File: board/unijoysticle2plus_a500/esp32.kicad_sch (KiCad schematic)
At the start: 17 parts, among them Q1 S8050, Q2 S8050, SW1 RESET, SW2 BOOT, U1 ESP32-WROOM-32E

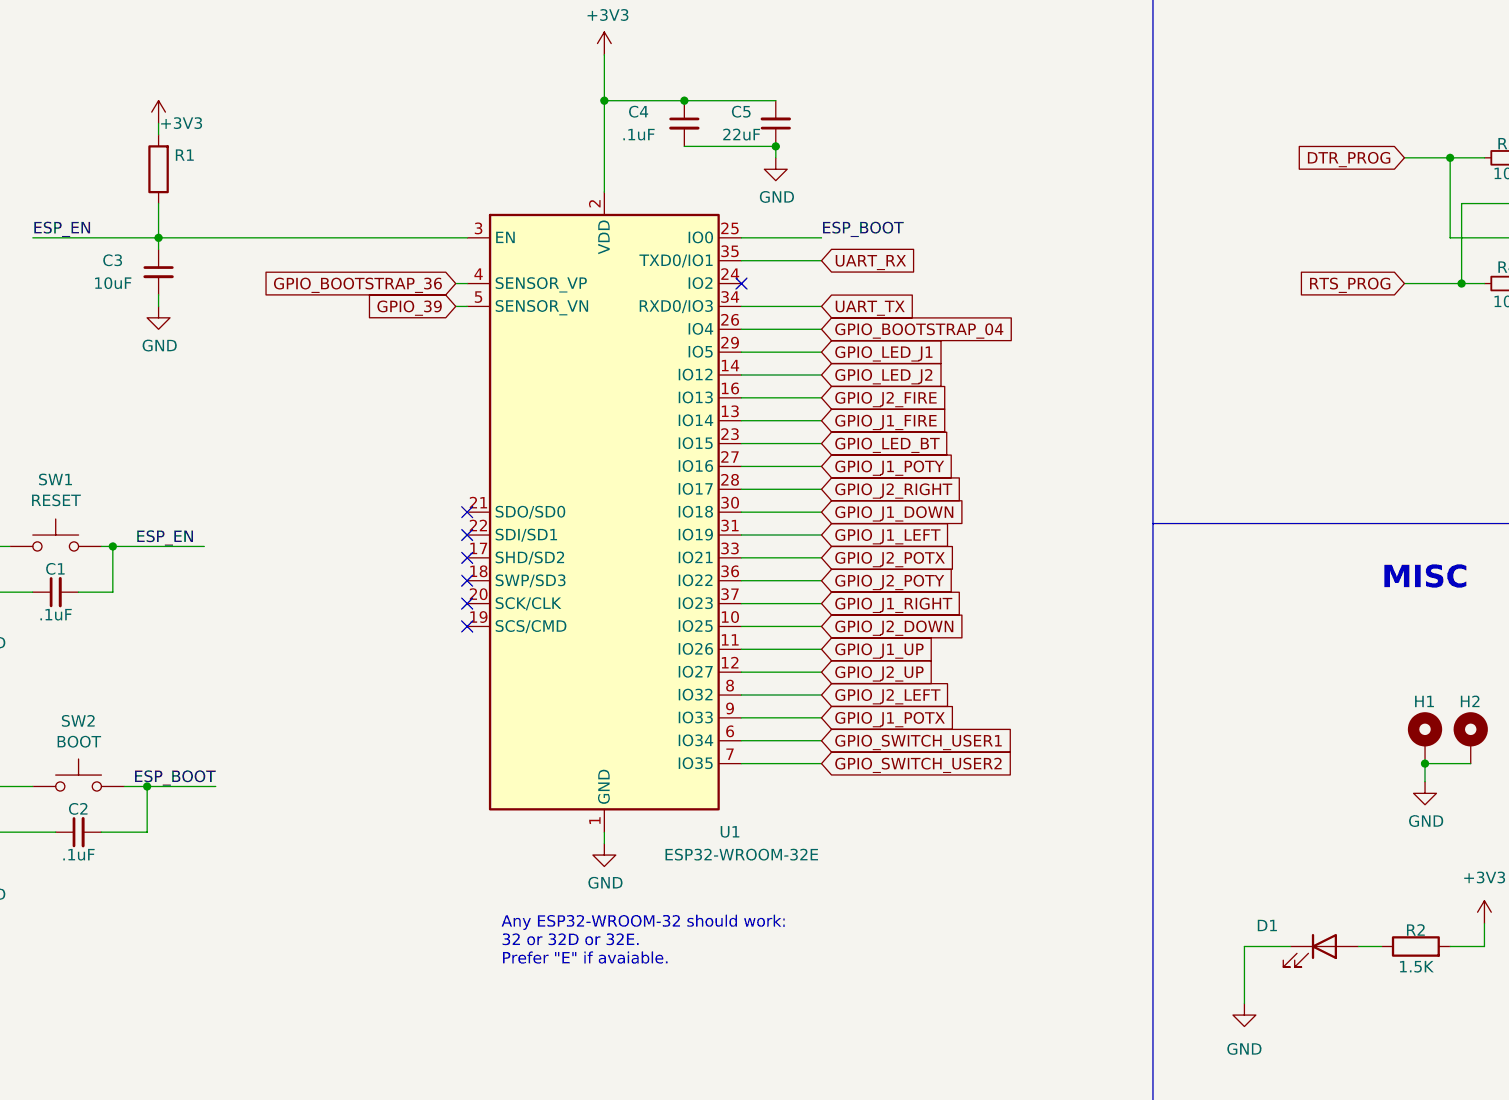
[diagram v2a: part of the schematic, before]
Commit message: uni a500: manual routing
WIP... all wires connected. requires to double check everything
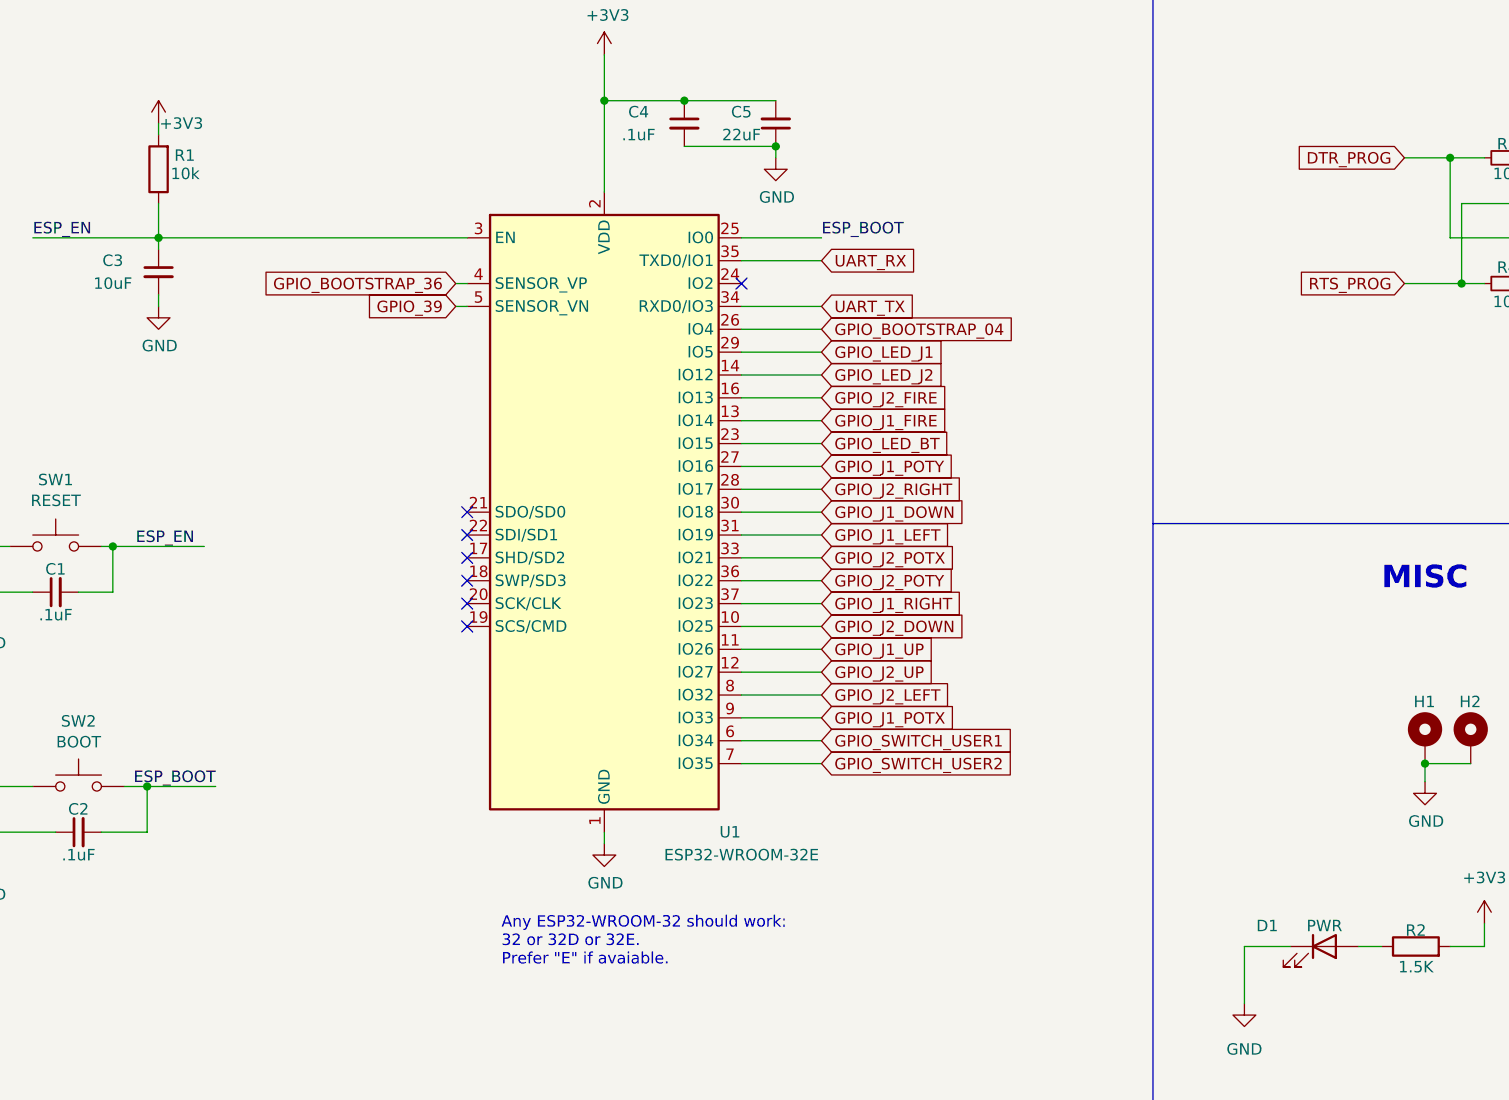
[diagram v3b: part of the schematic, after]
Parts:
- D1: value (none) -> PWR; footprint (none) -> LED_SMD:LED_0805_2012Metric_Pad1.15x1.40mm_HandSolder
- R1: value (none) -> 10k; footprint (none) -> Resistor_SMD:R_0805_2012Metric_Pad1.20x1.40mm_HandSolder
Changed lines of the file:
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@@
       (effects (font (size 1.27 1.27)) (justify left))
     )
-    (property "Value" "" (id 1) (at 42.672 44.958 0)
+    (property "Value" "10k" (id 1) (at 42.672 44.958 0)
       (effects (font (size 1.27 1.27)) (justify left))
     )
-    (property "Footprint" "" (id 2) (at 39.878 44.45 90)
+    (property "Footprint" "Resistor_SMD:R_0805_2012Metric_Pad1.20x1.40mm_HandSolder" (id 2) (at 39.878 44.45 90)
       (effects (font (size 1.27 1.27)) hide)
     )
@@
     (in_bom yes) (on_board yes)
     (property "Reference" "D1" (id 0) (at 161.29 128.524 0))
-    (property "Value" "" (id 1) (at 167.64 128.524 0))
-    (property "Footprint" "" (id 2) (at 167.64 130.81 0)
-      (effects (font (size 1.27 1.27)) hide)
-    )
+    (property "Value" "PWR" (id 1) (at 167.64 128.524 0))
+    (property "Footprint" "LED_SMD:LED_0805_2012Metric_Pad1.15x1.40mm_HandSolder" (id 2) (at 167.64 130.81 0)
+      (effects (font (size 1.27 1.27)) hide)
+    )

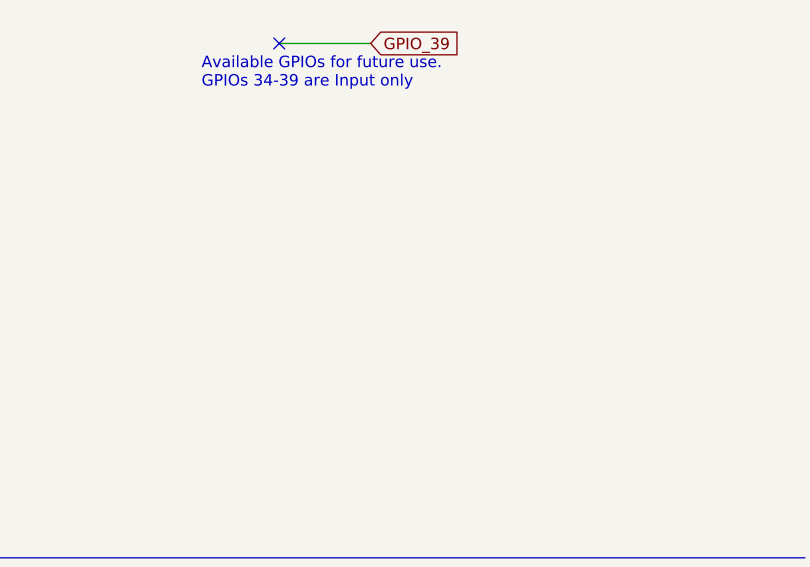
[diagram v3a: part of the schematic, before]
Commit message: Uni 2+ A500: many little changes
- replace resistor 0 with solder jumper for strapping pins
- move big cap a big down
- improved routing
- move vias outside pads
... and more
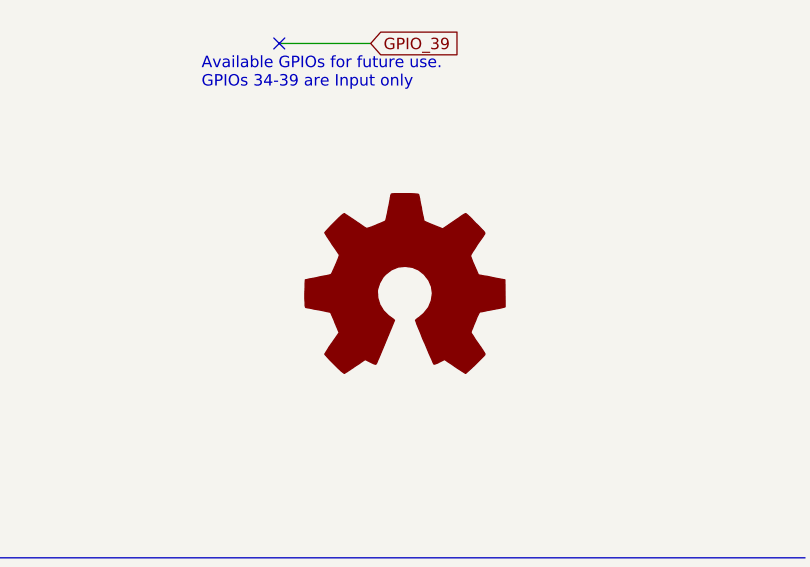
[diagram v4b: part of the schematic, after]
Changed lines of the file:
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@@
     (pin "1")
+  )
+  (symbol (lib_id "Graphic:Logo_Open_Hardware_Large") (at 240.03 124.46 0) (unit 1)
+    (in_bom yes) (on_board yes) (fields_autoplaced)
+    (property "Reference" "#LOGO1" (id 0) (at 240.03 111.76 0)
+      (effects (font (size 1.27 1.27)) hide)
+    )
+    (property "Value" "" (id 1) (at 240.03 134.62 0)
+      (effects (font (size 1.27 1.27)) hide)
+    )
+    (property "Footprint" "" (id 2) (at 240.03 124.46 0)
+      (effects (font (size 1.27 1.27)) hide)
+    )
+    (property "Datasheet" "~" (id 3) (at 240.03 124.46 0)
+      (effects (font (size 1.27 1.27)) hide)
+    )
   )
   (symbol (lib_id "power:GND") (at 158.75 137.16 0) (unit 1)

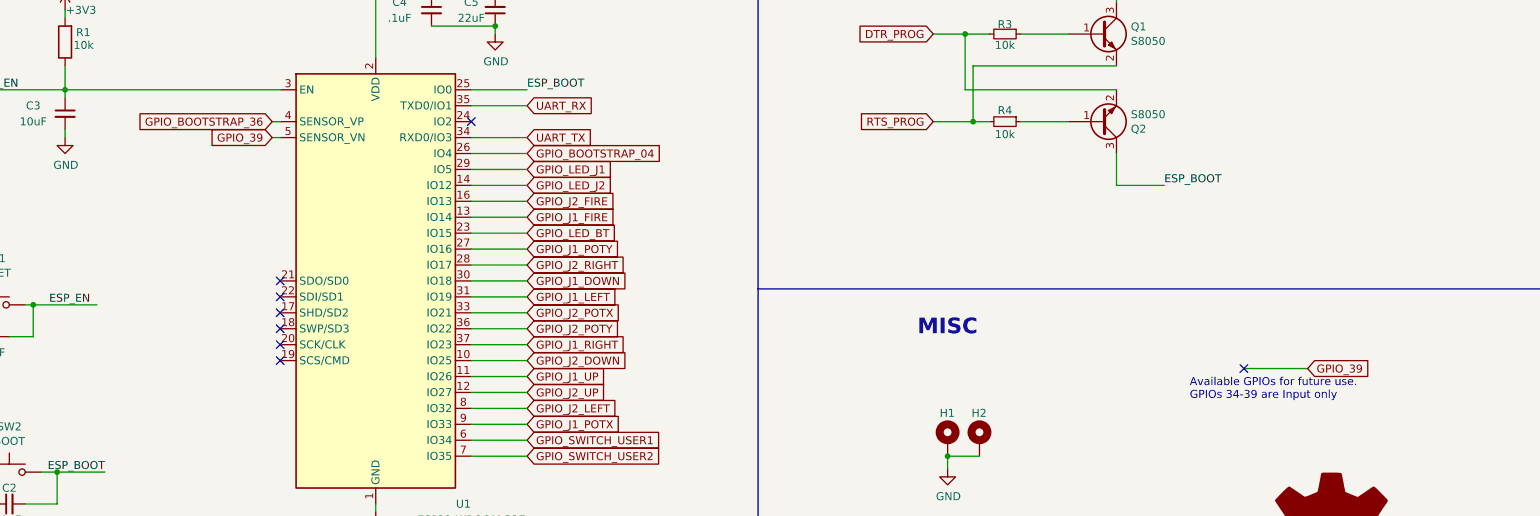
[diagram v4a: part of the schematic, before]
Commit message: A500: Reuse GPIO 15 both as LED and BoardId
Cannot use GPIOs 34~39 for Board ID since in previous models those leds
were floating and those GPIOs don't have pull-up/pull-down resistors.

To GPIO 15 is reused for board id and LEDs.

GPIO 36 and 39 and grounded for future-compatibility.

FIXME:Push buttons won't work. They require a pull-up/pull-down
resistor.
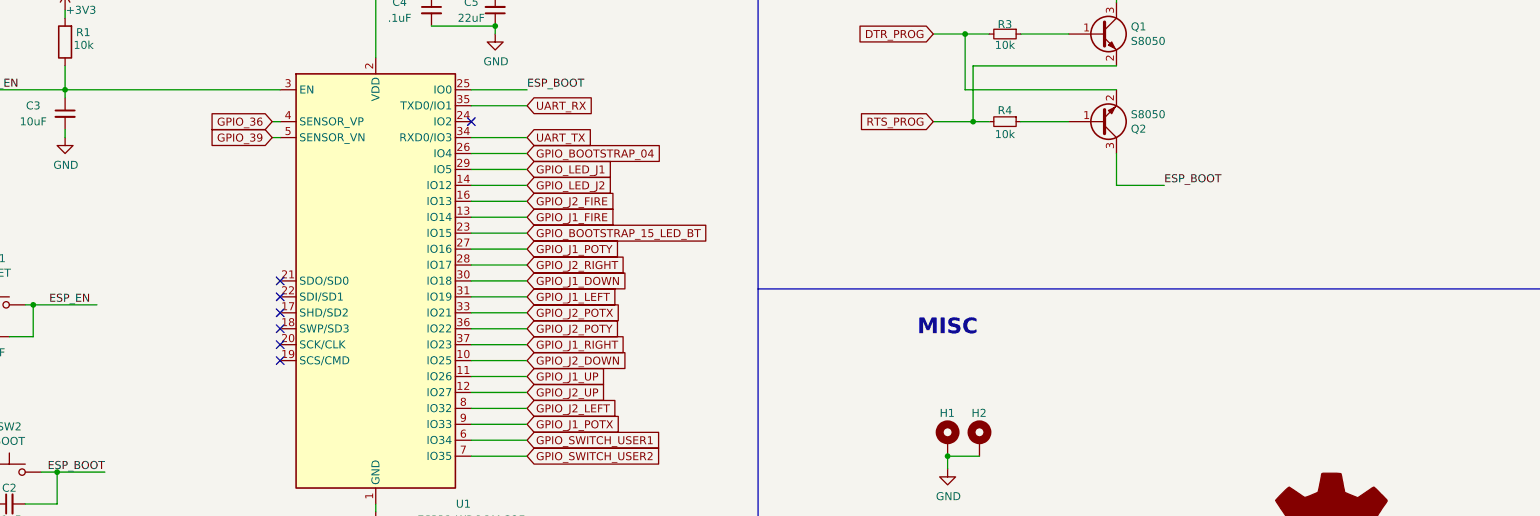
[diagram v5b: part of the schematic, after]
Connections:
- net GPIO_BOOTSTRAP_36 renamed GPIO_36
- net GPIO_LED_BT renamed GPIO_BOOTSTRAP_15_LED_BT
- no-connect marks 8 -> 7
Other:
- note removed: "Available GPIOs for future use. GPIOs 34-39 are Input only"
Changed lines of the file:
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@@
   (junction (at 19.05 91.44) (diameter 0) (color 0 0 0 0)
   )
-  (no_connect (at 226.06 96.52))
   (no_connect (at 72.39 92.71))
   (no_connect (at 72.39 90.17))
@@
     (stroke (width 0) (type default) (color 0 0 0 0))
   )
-  (wire (pts (xy 226.06 96.52) (xy 236.22 96.52))
-    (stroke (width 0) (type default) (color 0 0 0 0))
-  )
   (wire (pts (xy 102.87 85.09) (xy 111.76 85.09))
     (stroke (width 0) (type default) (color 0 0 0 0))
@@
   (text "AUTO RESET" (at 193.04 21.59 0)
     (effects (font (size 2.4892 2.4892) (thickness 0.4978) bold) (justify left bottom))
-  )
-  (text "Available GPIOs for future use.\nGPIOs 34-39 are Input only"
-    (at 217.424 101.6 0)
-    (effects (font (size 1.27 1.27)) (justify left bottom))
   )
   (label "ESP_BOOT" (at 44.45 113.03 180)
@@
     )
   )
-  (global_label "GPIO_LED_BT" (shape input) (at 111.76 74.93 0) (fields_autoplaced)
-    (effects (font (size 1.27 1.27)) (justify left))
-    (property "Intersheet References" "${INTERSHEET_REFS}" (id 0) (at 126.1794 74.8506 0)
+  (global_label "GPIO_BOOTSTRAP_15_LED_BT" (shape input) (at 111.76 74.93 0) (fields_autoplaced)
+    (effects (font (size 1.27 1.27)) (justify left))
+    (property "Intersheet References" "${INTERSHEET_REFS}" (id 0) (at 141.238 74.8506 0)
       (effects (font (size 1.27 1.27)) (justify left) hide)
     )
@@
     (effects (font (size 1.27 1.27)) (justify left))
     (property "Intersheet References" "${INTERSHEET_REFS}" (id 0) (at 133.4971 110.4106 0)
-      (effects (font (size 1.27 1.27)) (justify left) hide)
-    )
-  )
-  (global_label "GPIO_39" (shape input) (at 236.22 96.52 0) (fields_autoplaced)
-    (effects (font (size 1.27 1.27)) (justify left))
-    (property "Intersheet References" "${INTERSHEET_REFS}" (id 0) (at 246.4061 96.4406 0)
       (effects (font (size 1.27 1.27)) (justify left) hide)
     )
@@
     )
   )
-  (global_label "GPIO_BOOTSTRAP_36" (shape input) (at 71.12 57.15 180) (fields_autoplaced)
+  (global_label "GPIO_36" (shape input) (at 71.12 57.15 180) (fields_autoplaced)
     (effects (font (size 1.27 1.27)) (justify right))
-    (property "Intersheet References" "${INTERSHEET_REFS}" (id 0) (at 49.262 57.0706 0)
+    (property "Intersheet References" "${INTERSHEET_REFS}" (id 0) (at 60.9339 57.0706 0)
       (effects (font (size 1.27 1.27)) (justify right) hide)
     )
@@
       (effects (font (size 1.27 1.27)) hide)
     )
-    (property "Value" "" (id 1) (at 240.03 134.62 0)
-      (effects (font (size 1.27 1.27)) hide)
-    )
+    (property "Value" "Logo_Open_Hardware_Large" (id 1) (at 240.03 134.62 0)
+      (effects (font (size 1.27 1.27)) hide)
+    )

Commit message: Rename Uni2+ A500 to Uni2 A500
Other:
- title: Unijoysticle 2+ A500 -> Unijoysticle 2 A500
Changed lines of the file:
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@@
   (paper "A4")
   (title_block
-    (title "Unijoysticle 2+ A500")
-    (date "2022-04-20")
+    (title "Unijoysticle 2 A500")
+    (date "2022-04-25")
     (rev "A")
     (company "Retro Moe")
